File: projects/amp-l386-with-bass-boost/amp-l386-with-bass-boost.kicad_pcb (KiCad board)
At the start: 2 copper layers, 65 x 53.5 mm, 22 parts, among them U1 LM386

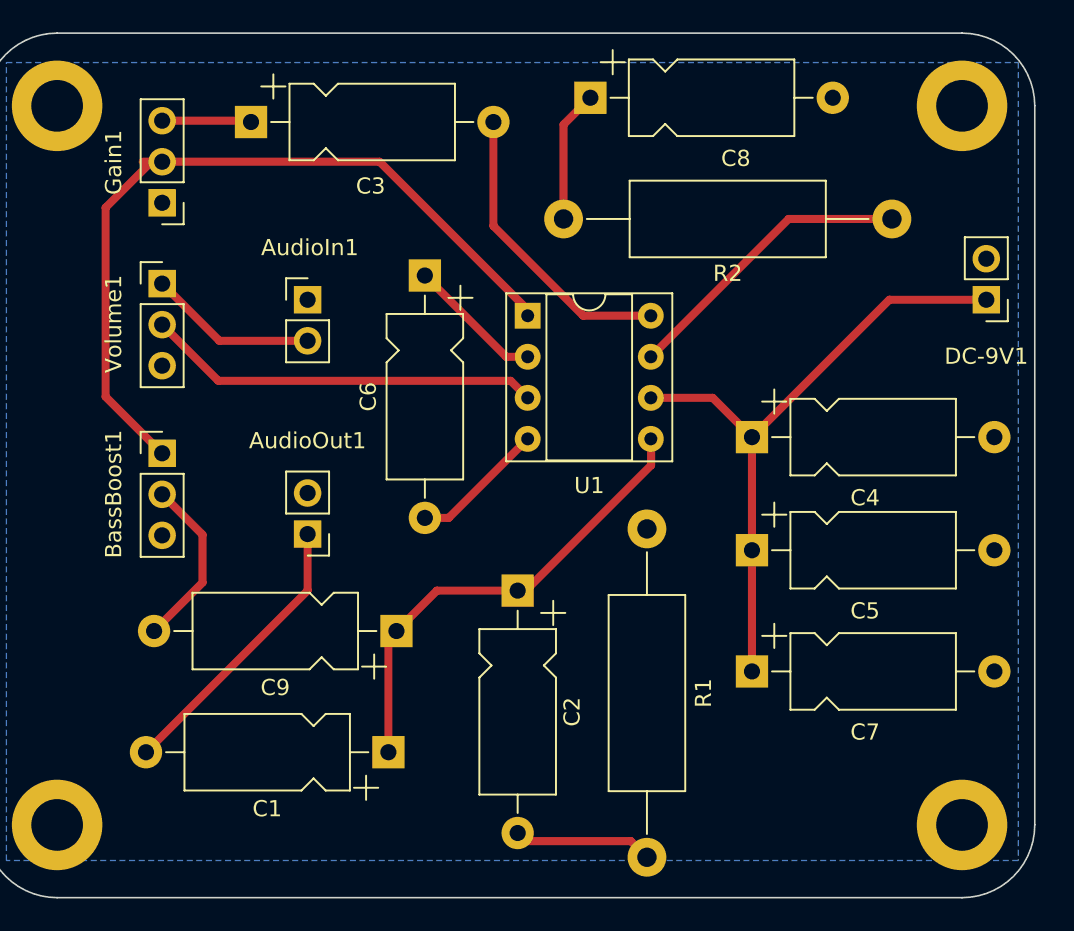
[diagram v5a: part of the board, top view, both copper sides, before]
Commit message: Correct several capacitor footprints (should be axial).
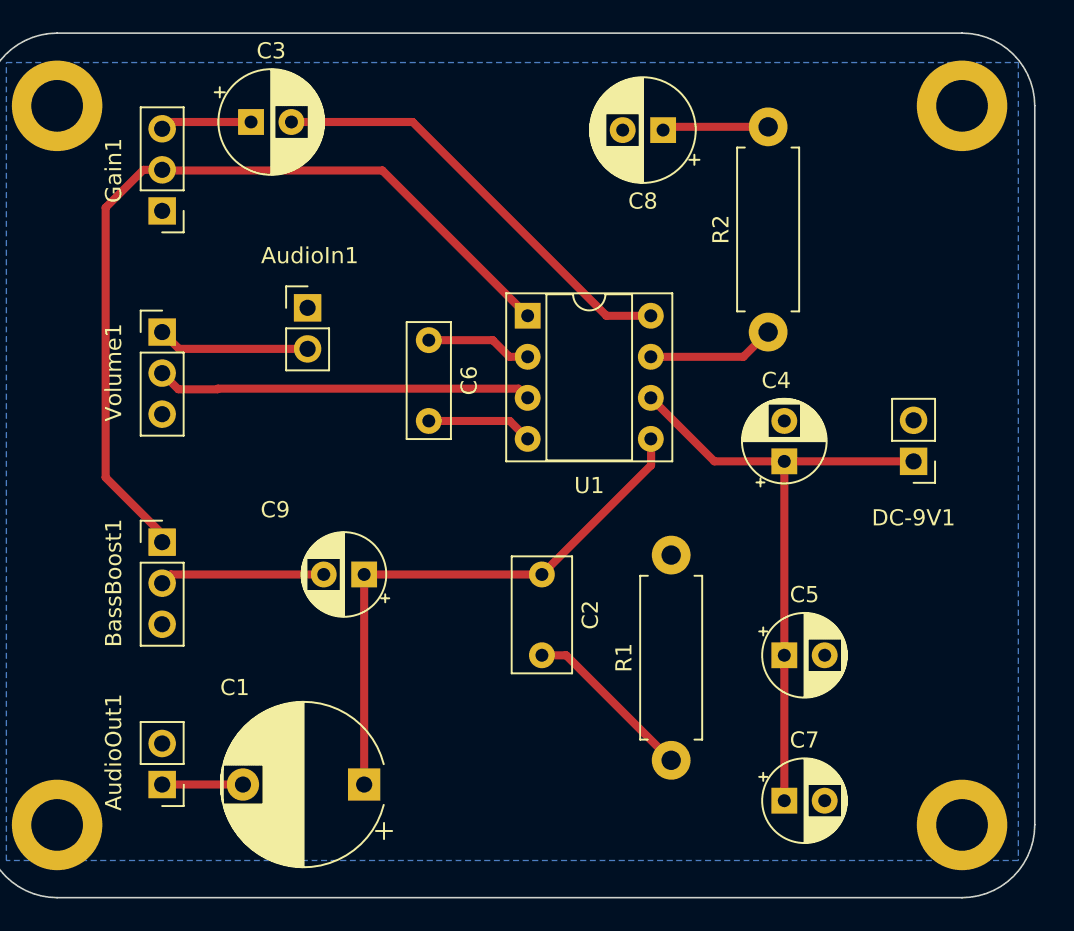
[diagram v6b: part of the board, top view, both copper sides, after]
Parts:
- C1: footprint Capacitor_THT:CP_Axial_L10.0mm_D4.5mm_P15.00mm_Horizontal -> Capacitor_THT:CP_Radial_D10.0mm_P7.50mm
- C2: footprint Capacitor_THT:CP_Axial_L10.0mm_D4.5mm_P15.00mm_Horizontal -> Capacitor_THT:C_Rect_L7.0mm_W3.5mm_P5.00mm
- C3, C8: footprint Capacitor_THT:CP_Axial_L10.0mm_D4.5mm_P15.00mm_Horizontal -> Capacitor_THT:CP_Radial_D6.3mm_P2.50mm
- C4, C5, C7, C9: footprint Capacitor_THT:CP_Axial_L10.0mm_D4.5mm_P15.00mm_Horizontal -> Capacitor_THT:CP_Radial_D5.0mm_P2.50mm
- C6: footprint Capacitor_THT:CP_Axial_L10.0mm_D4.5mm_P15.00mm_Horizontal -> Capacitor_THT:C_Rect_L7.0mm_W2.5mm_P5.00mm
- R1, R2: footprint Resistor_THT:R_Axial_DIN0414_L11.9mm_D4.5mm_P20.32mm_Horizontal -> Resistor_THT:R_Axial_DIN0411_L9.9mm_D3.6mm_P12.70mm_Horizontal
- moved AudioOut1 17.9 mm to (95.5, 139.5)
- moved DC-9V1 11.0 mm to (142.0, 119.5)
- moved R2 10.4 mm to (133.0, 111.5), turned to 90 degrees
- moved C7 8.25 mm to (134.0, 140.5)
- moved C5 6.80 mm to (134.0, 131.5)
- moved R1 6.18 mm to (127.0, 138.0)
- moved BassBoost1 5.50 mm to (95.5, 124.5)
- moved C8 4.92 mm to (126.5, 99.0), turned to 180 degrees
- moved C9 4.03 mm to (108.0, 126.5)
- moved C6 4.01 mm to (112.0, 112.0)
- moved Volume1 3.00 mm to (95.5, 111.5)
- moved C1 2.50 mm to (108.0, 139.5)
- moved C4 2.50 mm to (134.0, 119.5), turned to 90 degrees
- moved C2 1.80 mm to (119.0, 126.5)
- moved AudioIn1 0.50 mm to (104.5, 110.0)
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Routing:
- net Net-(AudioOut1-Pad1): track 17.6 -> 5.00 mm
- net Net-(R2-Pad1): track 18.5 -> 7.89 mm
- net Net-(C3-Pad2): track 18.5 -> 27.2 mm
- net Net-(C1-Pad1): track 29.4 -> 35.2 mm
- net GND: track 16.8 -> 13.1 mm
- net Net-(BassBoost1-Pad1): track 49.3 -> 53.0 mm
- net Net-(C2-Pad2): track 8.62 -> 10.7 mm
- net Net-(C8-Pad1): track 8.19 -> 6.58 mm
- net Net-(U1-Pad3): track 24.5 -> 23.3 mm
- net Net-(AudioIn1-PadT): track 10.5 -> 9.43 mm
- net +9V: track 39.8 -> 38.9 mm
- net Net-(BassBoost1-Pad2): track 10.7 -> 10.2 mm

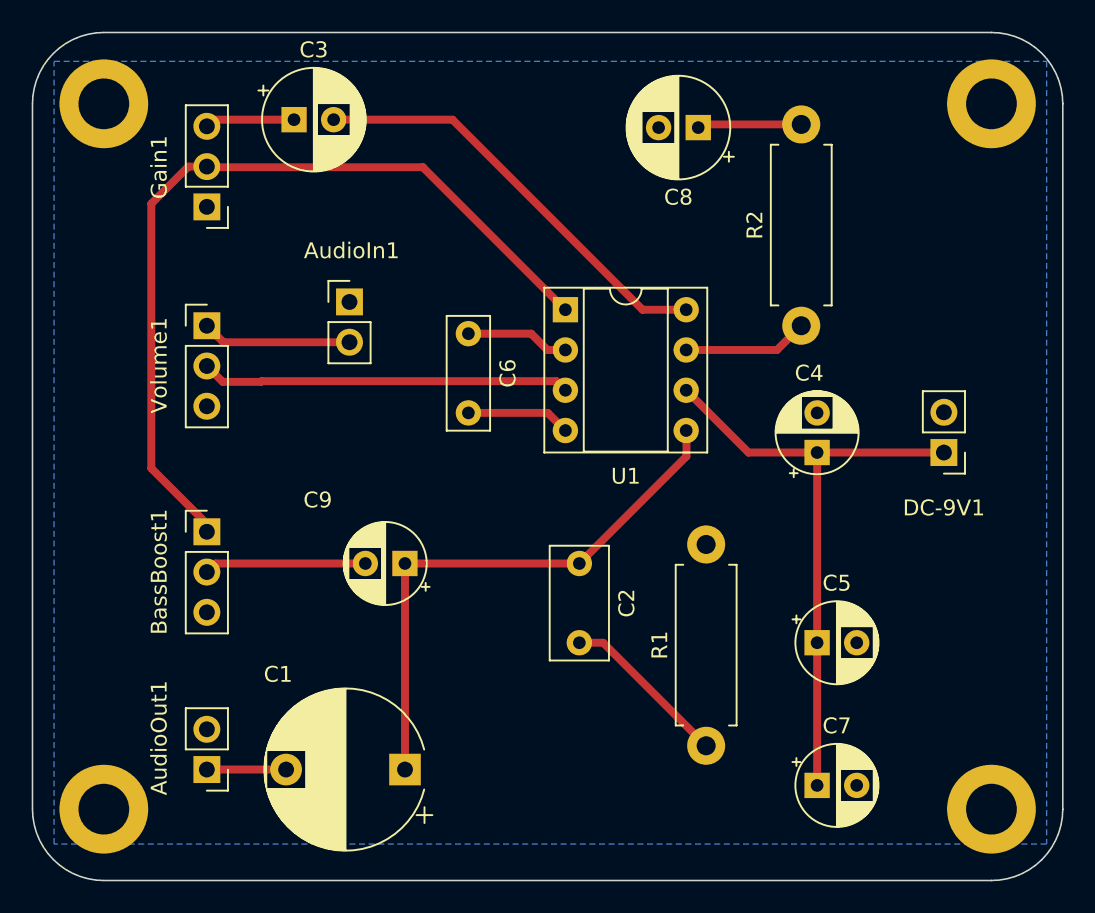
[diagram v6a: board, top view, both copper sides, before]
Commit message: Add test points
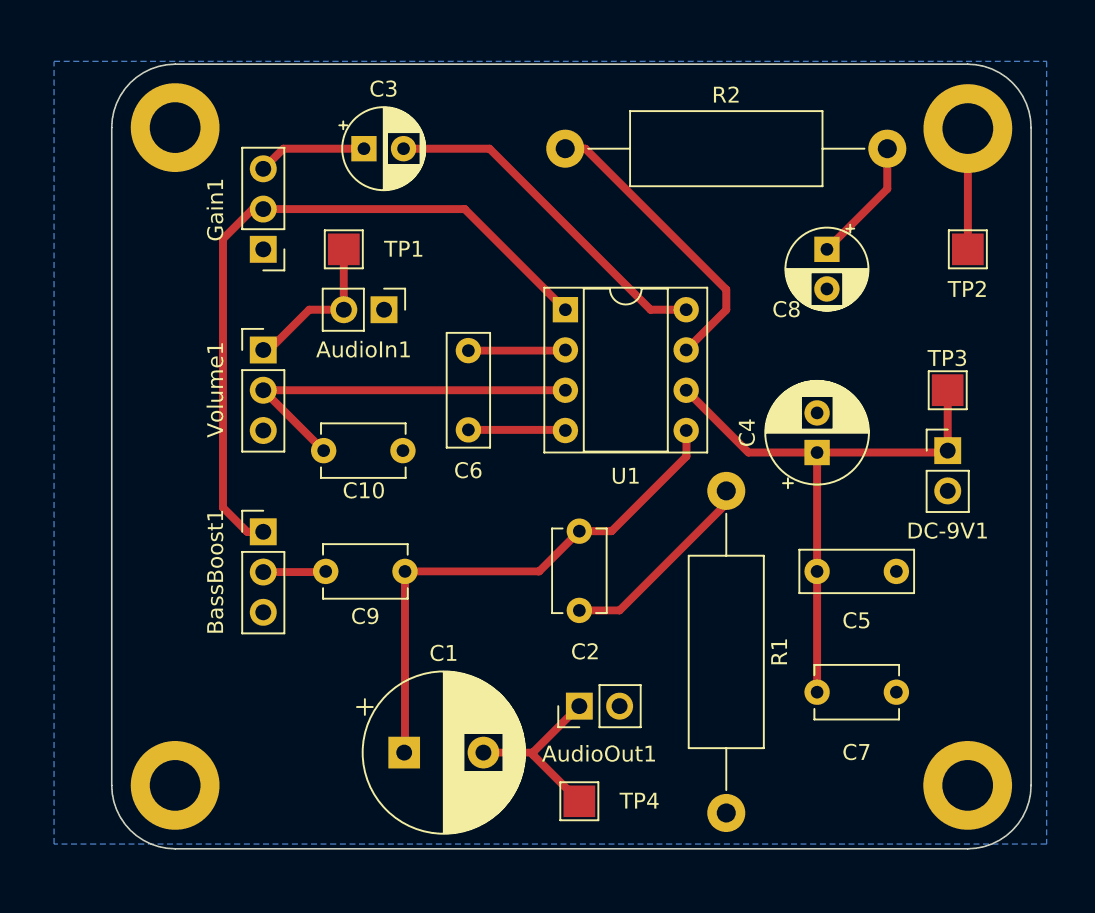
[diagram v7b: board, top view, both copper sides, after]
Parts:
- added C10: 47pF, Capacitor_THT:C_Disc_D5.1mm_W3.2mm_P5.00mm, F.Cu at (102.9, 119.4)
- added TP1: TestPoint, TestPoint:TestPoint_Pad_2.0x2.0mm, F.Cu at (104.1, 106.7)
- added TP2: TestPoint, TestPoint:TestPoint_Pad_2.0x2.0mm, F.Cu at (143.5, 106.7)
- added TP3: TestPoint, TestPoint:TestPoint_Pad_2.0x2.0mm, F.Cu at (142.2, 115.6)
- added TP4: TestPoint, TestPoint:TestPoint_Pad_2.0x2.0mm, F.Cu at (119.0, 141.5)
- C1: footprint Capacitor_THT:CP_Radial_D10.0mm_P7.50mm -> Capacitor_THT:CP_Radial_D10.0mm_P5.00mm
- C2: footprint Capacitor_THT:C_Rect_L7.0mm_W3.5mm_P5.00mm -> Capacitor_THT:C_Disc_D5.1mm_W3.2mm_P5.00mm
- C3, C8: footprint Capacitor_THT:CP_Radial_D6.3mm_P2.50mm -> Capacitor_THT:CP_Radial_D5.0mm_P2.50mm
- C4: footprint Capacitor_THT:CP_Radial_D5.0mm_P2.50mm -> Capacitor_THT:CP_Radial_D6.3mm_P2.50mm
- C5: footprint Capacitor_THT:CP_Radial_D5.0mm_P2.50mm -> Capacitor_THT:C_Rect_L7.0mm_W2.5mm_P5.00mm
- C6: value 470pF w/2&4 -> 470pF
- C7, C9: footprint Capacitor_THT:CP_Radial_D5.0mm_P2.50mm -> Capacitor_THT:C_Disc_D5.1mm_W3.2mm_P5.00mm
- R1, R2: footprint Resistor_THT:R_Axial_DIN0411_L9.9mm_D3.6mm_P12.70mm_Horizontal -> Resistor_THT:R_Axial_DIN0414_L11.9mm_D4.5mm_P20.32mm_Horizontal
- moved AudioOut1 23.8 mm to (119.0, 135.5), turned to 90 degrees
- moved R2 18.6 mm to (118.1, 100.3), turned to 0 degrees
- moved R1 16.1 mm to (128.3, 121.9), turned to -90 degrees
- moved C8 11.2 mm to (134.6, 106.7), turned to -90 degrees
- moved C6 6.07 mm to (112.0, 118.1), turned to 90 degrees
- moved C7 5.88 mm to (134.0, 134.6)
- moved C3 4.77 mm to (105.4, 100.3)
- moved H1 4.74 mm to (93.5, 140.5)
- moved H4 4.74 mm to (93.5, 99.0)
- moved C5 4.50 mm to (134.0, 127.0)
- moved Gain1 4.46 mm to (99.1, 106.7)
- moved Volume1 3.87 mm to (99.1, 113.0)
- moved BassBoost1 3.56 mm to (99.1, 124.5)
- moved AudioIn1 2.23 mm to (106.7, 110.5), turned to -90 degrees
- moved H3 2.16 mm to (143.5, 99.1)
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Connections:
- C6 pad 2: GND -> Net-(C6-Pad2)
- U1 pad 2: GND -> Net-(C6-Pad2)
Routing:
- net Net-(R2-Pad1): track 7.89 -> 18.7 mm
- net Net-(BassBoost1-Pad1): track 53.0 -> 45.1 mm
- net Net-(AudioOut1-Pad1): track 5.00 -> 11.5 mm
- net Net-(BassBoost1-Pad2): track 10.2 -> 3.96 mm
- net Net-(C6-Pad2): track 0.00 -> 6.14 mm
- net Net-(C3-Pad2): track 27.2 -> 22.0 mm
- net Net-(C2-Pad2): track 10.7 -> 12.9 mm
- net +9V: track 38.9 -> 37.1 mm
- net Net-(C8-Pad1): track 6.58 -> 7.93 mm
- net Net-(C1-Pad1): track 35.2 -> 33.9 mm
- net Net-(C3-Pad1): track 5.67 -> 6.88 mm
- net Net-(C10-Pad1): track 23.3 -> 24.4 mm
- net GND: track 13.1 -> 13.9 mm
- net Net-(AudioIn1-PadT): track 9.43 -> 9.94 mm
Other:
- board size 65 x 53.5 mm -> 58 x 49.5 mm
